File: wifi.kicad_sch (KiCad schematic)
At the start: 19 parts, among them P1 NP, Q1 2N7002, U1 SC16C550BIB48, U3 ESP-12E, Y1 24 MHz

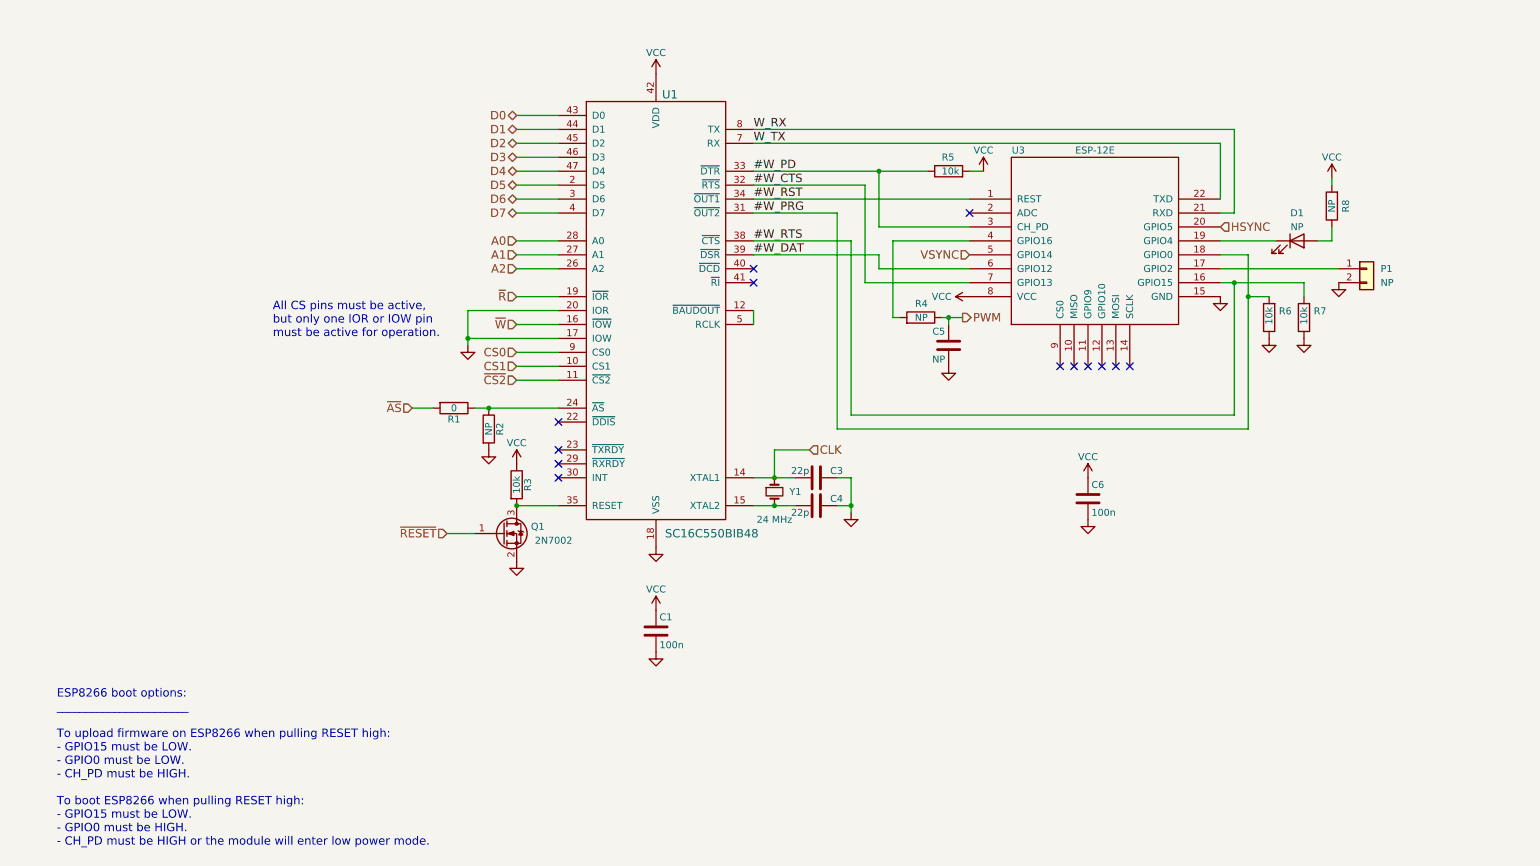
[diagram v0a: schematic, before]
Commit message: Update schematics for Rev.B:
* Switch obsolete SC16C554BIB48 with SC16C554BIBS
* Change ESP8266 with ESP32-C3
* Add USB-C connector for flashing/debugging
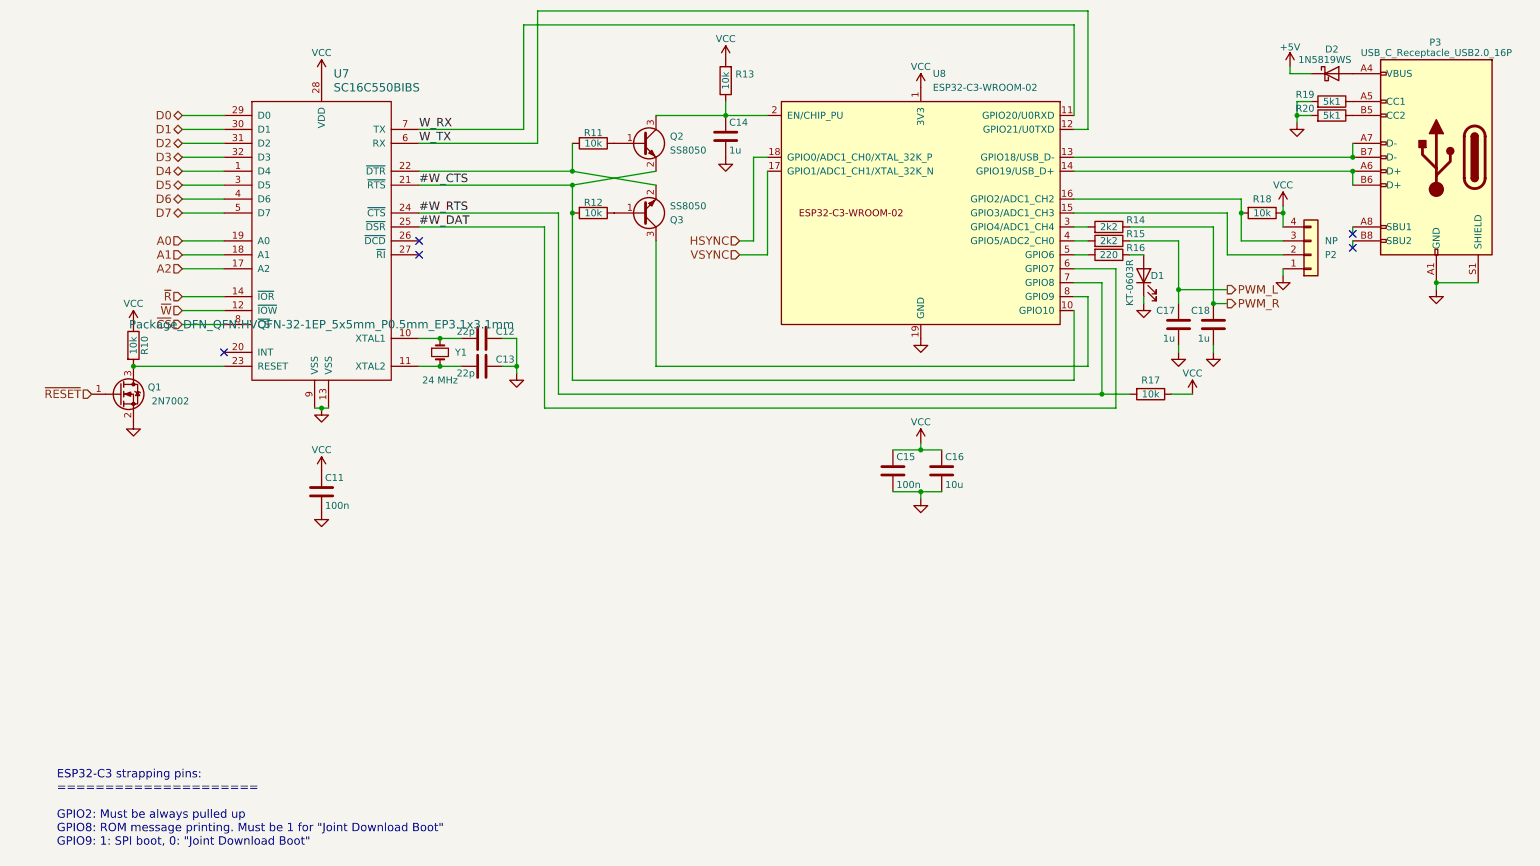
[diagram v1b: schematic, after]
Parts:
- removed C5: NP, Capacitors_SMD:C_0805, symbol Device:C
- removed R1: 0, doragasu:JUMPER_0805, symbol Device:R
- removed R2, R4: NP, Resistors_SMD:R_0805, symbol Device:R
- removed R5: 10k, Resistors_SMD:R_0805, symbol Device:R
- removed U1: SC16C550BIB48, Housings_QFP:TQFP-48_7x7mm_Pitch0.5mm, symbol doragasu:SC16C550BIB48
- removed U3: ESP-12E, ESP8266:ESP-12E, symbol ESP8266:ESP-12E
- added C14, C17, C18: 1u, Capacitor_SMD:C_0805_2012Metric, symbol Device:C
- added C16: 10u, Capacitor_SMD:C_0805_2012Metric, symbol Device:C
- added D2: 1N5819WS, Diode_SMD:D_SOD-323, symbol Diode:1N5819WS
- added P3: USB_C_Receptacle_USB2.0_16P, Connector_USB:USB_C_Receptacle_HCTL_HC-TYPE-C-16P-01A, symbol Connector:USB_C_Receptacle_USB2.0_16P
- added Q2, Q3: SS8050, Package_TO_SOT_SMD:SOT-23, symbol Device:Q_NPN_BEC
- added R12, R17, R18: 10k, Resistor_SMD:R_0603_1608Metric, symbol Device:R
- added R14, R15: 2k2, Resistor_SMD:R_0603_1608Metric, symbol Device:R
- added R19, R20: 5k1, Resistor_SMD:R_0402_1005Metric, symbol Device:R
- added U7: SC16C550BIBS, Package_DFN_QFN:HVQFN-32-1EP_5x5mm_P0.5mm_EP3.1x3.1mm, symbol doragasu:SC16C550BIBS
- added U8: ESP32-C3-WROOM-02, PCM_Espressif:ESP32-C3-WROOM-02, symbol PCM_Espressif:ESP32-C3-WROOM-02
- C11: renamed from C1; footprint Capacitors_SMD:C_0805 -> Capacitor_SMD:C_0603_1608Metric; LCSC# C2830722 -> C14663
- C12: renamed from C3; footprint Capacitors_SMD:C_0805 -> Capacitor_SMD:C_0603_1608Metric; LCSC# C237185 -> C1653
- C13: renamed from C4; footprint Capacitors_SMD:C_0805 -> Capacitor_SMD:C_0603_1608Metric; LCSC# C237185 -> C1653
- C15: renamed from C6; footprint Capacitors_SMD:C_0805 -> Capacitor_SMD:C_0603_1608Metric; LCSC# C2830722 -> C14663
- D1: value NP -> KT-0603R; LCSC# (none) -> C2286
- P2: renamed from P1; footprint Connector_PinHeader_2.54mm:PinHeader_1x02_P2.54mm_Vertical -> Connector_PinHeader_2.54mm:PinHeader_1x04_P2.54mm_Vertical; symbol Connector_Generic:Conn_01x02 -> Connector_Generic:Conn_01x04
- Q1: LCSC# C306856 -> C8545
- R10: renamed from R3; footprint Resistors_SMD:R_0805 -> Resistor_SMD:R_0603_1608Metric; LCSC# C2763777 -> C25804
- R11: renamed from R6; footprint Resistors_SMD:R_0805 -> Resistor_SMD:R_0603_1608Metric; LCSC# C2763777 -> C25804
- R13: renamed from R7; footprint Resistors_SMD:R_0805 -> Resistor_SMD:R_0603_1608Metric; LCSC# C2763777 -> C25804
- R16: renamed from R8; value NP -> 220; footprint Resistors_SMD:R_0805 -> Resistor_SMD:R_0603_1608Metric; LCSC# (none) -> C22962
- Y1: footprint Crystals:Crystal_HC49-SD_SMD -> Crystal:Crystal_SMD_HC49-SD
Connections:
- net #W_CTS: now also Q2.2 (E), R12.2, U7.21 (~{RTS}), U8.10 (GPIO10)
- net #W_DAT: now also U7.25 (~{DSR}), U8.6 (GPIO7)
- net #W_RTS: now also R17.2, U7.24 (~{CTS}), U8.7 (GPIO8); no longer R13.2
- net A0: now also U7.19 (A0)
- net A1: now also U7.18 (A1)
- net A2: now also U7.17 (A2)
- net D0: now also U7.29 (D0)
- net D1: now also U7.30 (D1)
- net D2: now also U7.31 (D2)
- net D3: now also U7.32 (D3)
- net D4: now also U7.1 (D4)
- net D5: now also U7.3 (D5)
- net D6: now also U7.4 (D6)
- net D7: now also U7.5 (D7)
- net GND: now also D1.1 (K), P2.1 (Pin_1), C14.2, C16.2, C17.2, C18.2, P3.A1 (GND), P3.A12 (GND), P3.B1 (GND), P3.B12 (GND), P3.S1 (SHIELD), R19.2, R20.2, U7.13 (VSS), U7.9 (VSS), U8.19 (GND), U8.9 (GND); no longer P2.2 (Pin_2), R11.1, R13.1
- net HSYNC: now also U8.18 (GPIO0/ADC1_CH0/XTAL_32K_P)
- net VCC: now also P2.4 (Pin_4), R13.2, C16.1, R17.1, R18.1, U7.28 (VDD), U8.1 (3V3); no longer R16.2
- net VSYNC: now also U8.17 (GPIO1/ADC1_CH1/XTAL_32K_N)
- net W_RX: now also U7.7 (TX), U8.11 (GPIO20/U0RXD)
- net W_TX: now also U7.6 (RX), U8.12 (GPIO21/U0TXD)
- net ~{R}: now also U7.14 (~{IOR})
- net ~{W}: now also U7.12 (~{IOW})
- net at C13.2, Y1.2: now also U7.11 (XTAL2)
- net at Q1.3 (D), R10.2: now also U7.23 (RESET)
- net #W_PRG: no longer names the net of R11.2
- net #W_PRG: now also Q3.2 (E), U7.22 (~{DTR})
- net CLK: no longer names the net of C12.2, Y1.1
- net CLK: now also U7.10 (XTAL1)
- new net: R16.2, U8.5 (GPIO6)
- new net: C14.1, Q2.3 (C), R13.1, U8.2 (EN/CHIP_PU)
- new net: Q2.1 (B), R11.1
- new net: P2.2 (Pin_2), U8.15 (GPIO3/ADC1_CH3)
- new net: P2.3 (Pin_3), R18.2, U8.16 (GPIO2/ADC1_CH2)
- new net: D2.2 (A), P3.A4 (VBUS), P3.A9 (VBUS), P3.B4 (VBUS), P3.B9 (VBUS)
- new net: P3.A5 (CC1), R19.1
- new net: R14.2, U8.3 (GPIO4/ADC1_CH4)
- new net: Q3.1 (B), R12.1
- new net: Q3.3 (C), U8.8 (GPIO9)
- new net: P3.A6 (D+), P3.B6 (D+), U8.14 (GPIO19/USB_D+)
- new net: P3.A7 (D-), P3.B7 (D-), U8.13 (GPIO18/USB_D-)
- new net: P3.B5 (CC2), R20.1
- new net: R15.2, U8.4 (GPIO5/ADC2_CH0)
- new net +5V: D2.1 (K)
- new net PWM_L: C17.1, R15.1
- new net PWM_R: C18.1, R14.1
- new net ~{CS}: U7.8 (~{CS})
- no-connect marks 13 -> 5
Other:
- note added: "ESP32-C3 strapping pins: ===================== GPIO2: Must be always pulled up GPIO8: ROM message printing. Must be 1 for "Joint Download Boot" GPIO9: 1: SPI boot, 0: "Joint Download Boot""
- note removed: "All CS pins must be active, but only one IOR or IOW pin must be active for operation."
- note removed: "ESP8266 boot options: _______________________ To upload firmware on ESP8266 when pulling RESET high: - GPIO15 must be LOW. - GPIO0 must be LOW. - CH_PD must be HIGH. To boot ESP8266 when pulling RESET high: - GPIO15 must be LOW. - GPIO0 must be HIGH. - CH_PD must be HIGH or the module will enter low power mode."
- moved on the sheet: C11, C12, C13, C15, D1, Q1, R10, R11, R13, R16, Y1

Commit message: Rev.B PCB
* Replace obsolete SC16C550BIB48 with SC16C550BIBS
* Replace ESP8266 with ESP32-C3
* Implement 64 Mbit hack
* Add USB-C debug header for ESP32-C3
* Many PCB improvements
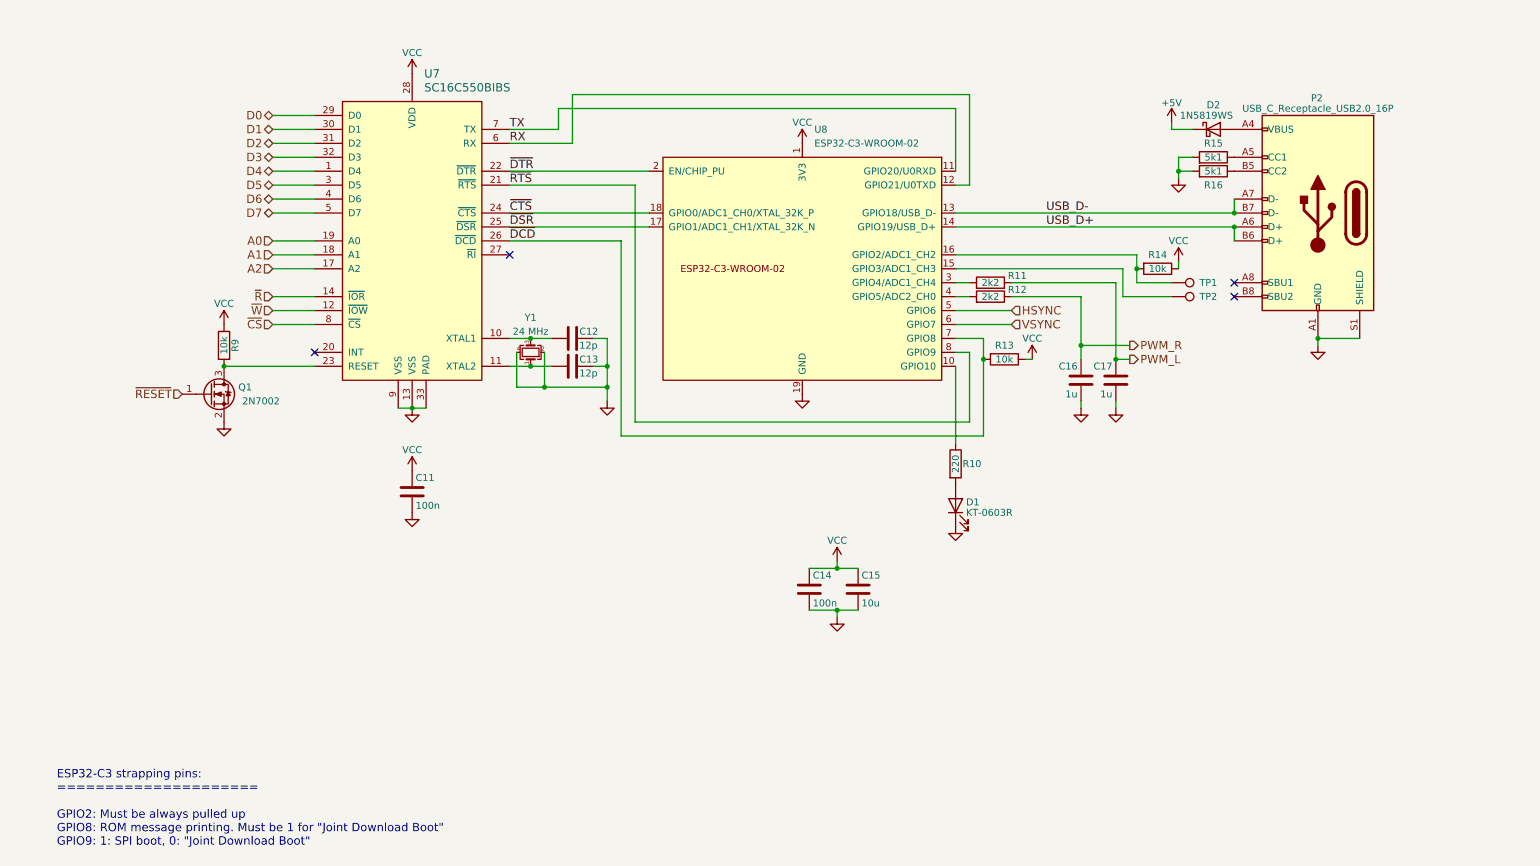
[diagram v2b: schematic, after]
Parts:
- removed C14: 1u, Capacitor_SMD:C_0805_2012Metric, symbol Device:C
- removed P2: NP, Connector_PinHeader_2.54mm:PinHeader_1x04_P2.54mm_Vertical, symbol Connector_Generic:Conn_01x04
- removed Q2, Q3: SS8050, Package_TO_SOT_SMD:SOT-23, symbol Device:Q_NPN_BEC
- removed R11, R12, R13: 10k, Resistor_SMD:R_0603_1608Metric, symbol Device:R
- removed Y1: 24 MHz, Crystal:Crystal_SMD_HC49-SD, symbol Device:Crystal_Small
- added TP1, TP2: TestPoint, TestPoint:TestPoint_Pad_D1.0mm, symbol Connector:TestPoint
- added Y1: 24 MHz, Crystal:Crystal_SMD_2520-4Pin_2.5x2.0mm, symbol Device:Crystal_GND24_Small
- C12, C13: value 22p -> 12p; LCSC# C1653 -> C38523
- C16: renamed from C18; LCSC# C2830722 -> C28323
- C17: LCSC# C2830722 -> C28323
- D1: footprint LEDs:LED-0603 -> LED_SMD:LED_0603_1608Metric
- Q1: footprint Transistors_SMD:sot23 -> Package_TO_SOT_SMD:SOT-23
- renumbered C15 to C14, C16 to C15, P3 to P2, R16 to R10, R15 to R11, R14 to R12, R17 to R13, R18 to R14, R19 to R15, R20 to R16, R10 to R9
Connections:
- net GND: now also U7.33 (PAD), Y1.2, Y1.4
- net HSYNC: now also U8.5 (GPIO6); no longer U8.18 (GPIO0/ADC1_CH0/XTAL_32K_P)
- net VSYNC: now also U8.6 (GPIO7); no longer U8.17 (GPIO1/ADC1_CH1/XTAL_32K_N)
- net at C12.2, U7.10 (XTAL1): now also Y1.3
- net at C13.2, U7.11 (XTAL2): now also Y1.1
- net at R10.1: now also U8.10 (GPIO10); no longer D1.2 (A)
- net at R10.2: now also D1.2 (A); no longer U8.5 (GPIO6)
- net ~{DTR}: now reaches U8.2 (EN/CHIP_PU)
- net ~{DTR}: now also U7.22 (~{DTR})
- net at U8.15 (GPIO3/ADC1_CH3): now also TP2.1
- net at R14.2, U8.16 (GPIO2/ADC1_CH2): now also TP1.1
- net ~{DCD}: now reaches U7.26 (~{DCD})
- net ~{DCD}: now also R13.2, U8.7 (GPIO8)
- net at R12.2: now also U8.4 (GPIO5/ADC2_CH0); no longer U8.3 (GPIO4/ADC1_CH4)
- net ~{RTS}: now reaches U8.8 (GPIO9)
- net ~{RTS}: now also U7.21 (~{RTS})
- net USB_D+: now reaches P2.A6 (D+), P2.B6 (D+), U8.14 (GPIO19/USB_D+)
- net USB_D-: now reaches P2.A7 (D-), P2.B7 (D-), U8.13 (GPIO18/USB_D-)
- net at R11.2: now also U8.3 (GPIO4/ADC1_CH4); no longer U8.4 (GPIO5/ADC2_CH0)
- removed net #W_CTS: U7.21 (~{RTS}), U8.10 (GPIO10)
- net #W_DAT renamed ~{DSR}
- net ~{DSR}: now also U8.17 (GPIO1/ADC1_CH1/XTAL_32K_N); no longer U8.6 (GPIO7)
- removed net #W_RTS: R13.2, U7.24 (~{CTS}), U8.7 (GPIO8)
- net W_RX renamed TX
- net W_TX renamed RX
- new net ~{CTS}: U7.24 (~{CTS}), U8.18 (GPIO0/ADC1_CH0/XTAL_32K_P)
- no-connect marks 5 -> 4
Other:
- moved on the sheet: C11, C12, C13, C14, C15, C16, C17, D1, D2, P2, Q1, R10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

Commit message: Fabrication tweaks
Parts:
- C16, C17, D1, R10, R11, R12, R15, R16: Config DNF -> (none)
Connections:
- net GND: now also R15.1, R16.1; no longer R15.2, R16.2
- net PWM_L: now also R11.2; no longer R11.1
- net PWM_R: now also R12.2; no longer R12.1
- net at P2.A5 (CC1): now also R15.2; no longer R15.1
- net at U8.4 (GPIO5/ADC2_CH0): now also R12.1; no longer R12.2
- net at P2.B5 (CC2): now also R16.2; no longer R16.1
- net at U8.3 (GPIO4/ADC1_CH4): now also R11.1; no longer R11.2
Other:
- note added: "ESP32-C3 strapping pins: ================ GPIO2: Must be always pulled up GPIO8: ROM message printing. Must be 1 for "Joint Download Boot" GPIO9: 1: SPI boot, 0: "Joint Download Boot" Boot sequences: ========== * Normal (SPI) boot: clear ~{DTR}, set ~{RTS}, set ~{DTR} * Joint download boot: clear ~{DTR}, clear ~{RTS}, set ~{DTR}"
- note removed: "ESP32-C3 strapping pins: ===================== GPIO2: Must be always pulled up GPIO8: ROM message printing. Must be 1 for "Joint Download Boot" GPIO9: 1: SPI boot, 0: "Joint Download Boot""
